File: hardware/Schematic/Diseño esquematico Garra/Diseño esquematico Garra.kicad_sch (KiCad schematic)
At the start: 14 parts, among them U2 ESP32-WROOM-32

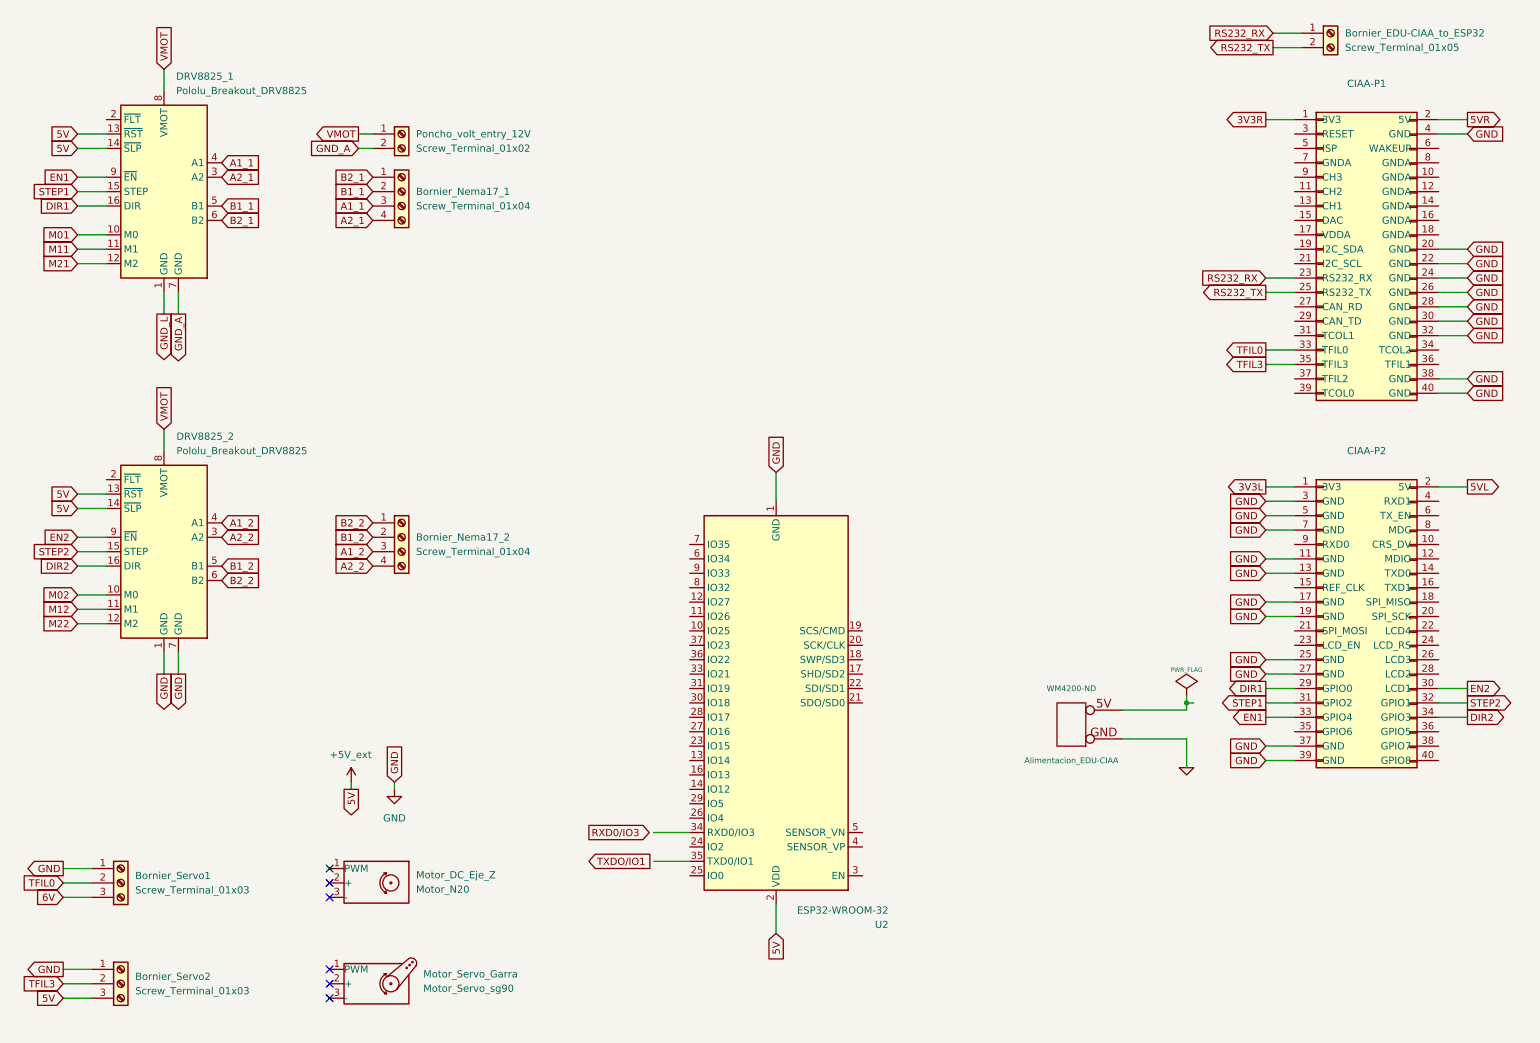
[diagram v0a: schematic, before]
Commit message: Schematics updated - pins, PowerSupply
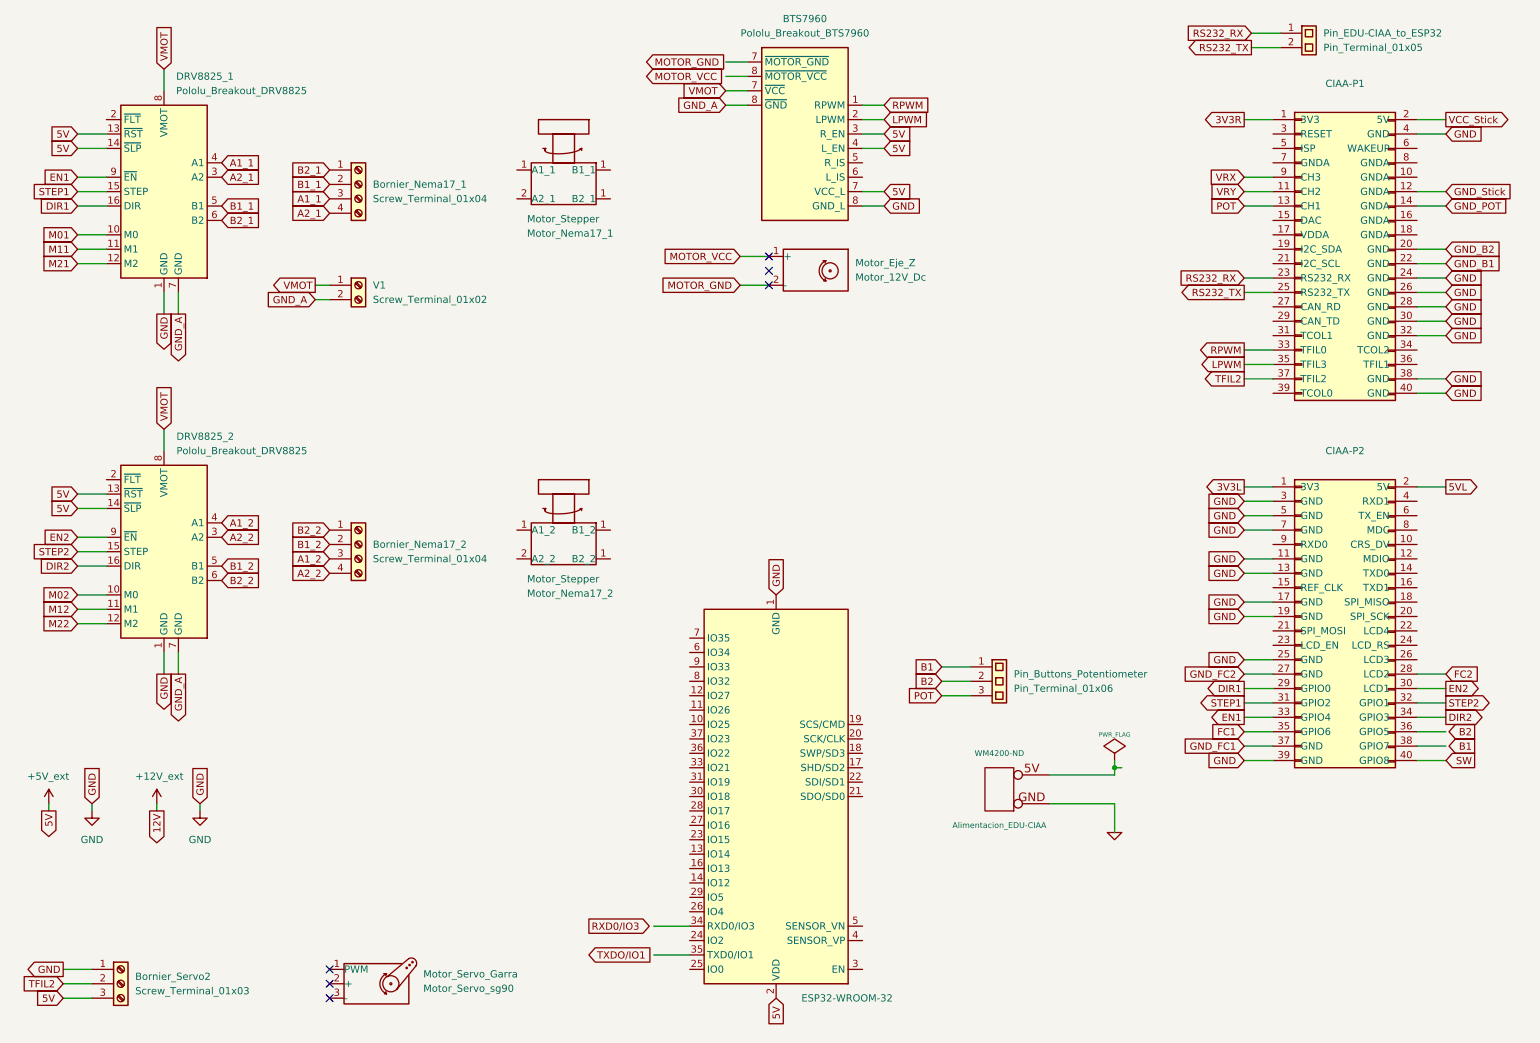
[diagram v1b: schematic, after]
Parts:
- removed Bornier_Servo1: Screw_Terminal_01x03, ProyectoTdL:TerminalBlock_bornier-3_P5.08mm, symbol Connector:Screw_Terminal_01x03
- added BTS7960: Pololu_Breakout_BTS7960, Module:Pololu_Breakout-16_15.2x20.3mm, symbol Driver_Motor:Pololu_Breakout_DRV8825
- added Motor_Stepper: Motor_Nema17_2, symbol Motor:Motor_Servo
- added Motor_Stepper: Motor_Nema17_1, symbol Motor:Motor_Servo
- added Pin_Buttons_Potentiometer: Pin_Terminal_01x06, ProyectoTdL:TerminalBlock_bornier-3_P5.08mm, symbol Connector:Screw_Terminal_01x03
- Motor_Eje_Z: renamed from Motor_DC_Eje_Z; value Motor_N20 -> Motor_12V_Dc
- Pin_EDU-CIAA_to_ESP32: renamed from Bornier_EDU-CIAA_to_ESP32; value Screw_Terminal_01x05 -> Pin_Terminal_01x05
- renumbered Poncho_volt_entry_12V to V1
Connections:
- net GND_L is gone; now on net GND: DRV8825_1.1 (GND)
- net +5V_ext: now also BTS7960.3 (R_EN), BTS7960.4 (L_EN), BTS7960.7 (VCC_L)
- net GND: now also BTS7960.8 (GND_L); no longer CIAA-P1.20 (GND), CIAA-P1.22 (GND), CIAA-P2.27 (GND), CIAA-P2.37 (GND), DRV8825_2.7 (GND)
- net GND_A: now also DRV8825_2.7 (GND), BTS7960.8 (GND_L)
- net VMOT: now also BTS7960.7 (VCC_L)
- net VRY: now reaches CIAA-P1.11 (CH2)
- net GND_Stick: now reaches CIAA-P1.12 (GNDA)
- net POT: now reaches CIAA-P1.13 (CH1)
- net POT: now also Pin_Buttons_Potentiometer.3 (Pin_3)
- net GND_POT: now reaches CIAA-P1.14 (GNDA)
- net TFIL2: now reaches CIAA-P1.37 (TFIL2)
- net TFIL2: now also Bornier_Servo2.2 (Pin_2)
- net VRX: now reaches CIAA-P1.9 (CH3)
- net MOTOR_VCC: now reaches Motor_Eje_Z.1 (+)
- net MOTOR_GND: now reaches Motor_Eje_Z.2 (-)
- net FC2: now reaches CIAA-P2.28 (LCD2)
- net FC1: now reaches CIAA-P2.35 (GPIO6)
- net 5VR renamed VCC_Stick
- net TFIL0 renamed RPWM
- net RPWM: now also BTS7960.1 (RPWM)
- net TFIL3 renamed LPWM
- net LPWM: now also BTS7960.2 (LPWM); no longer Bornier_Servo2.2 (Pin_2)
- new net B1: Pin_Buttons_Potentiometer.1 (Pin_1)
- new net B2: Pin_Buttons_Potentiometer.2 (Pin_2)
- new net GND_B1: CIAA-P1.22 (GND)
- new net GND_B2: CIAA-P1.20 (GND)
- new net GND_FC1: CIAA-P2.37 (GND)
- new net GND_FC2: CIAA-P2.27 (GND)
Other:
- moved on the sheet: Alimentacion_EDU-CIAA, Bornier_Nema17_1, Bornier_Nema17_2, CIAA-P1, CIAA-P2, V1

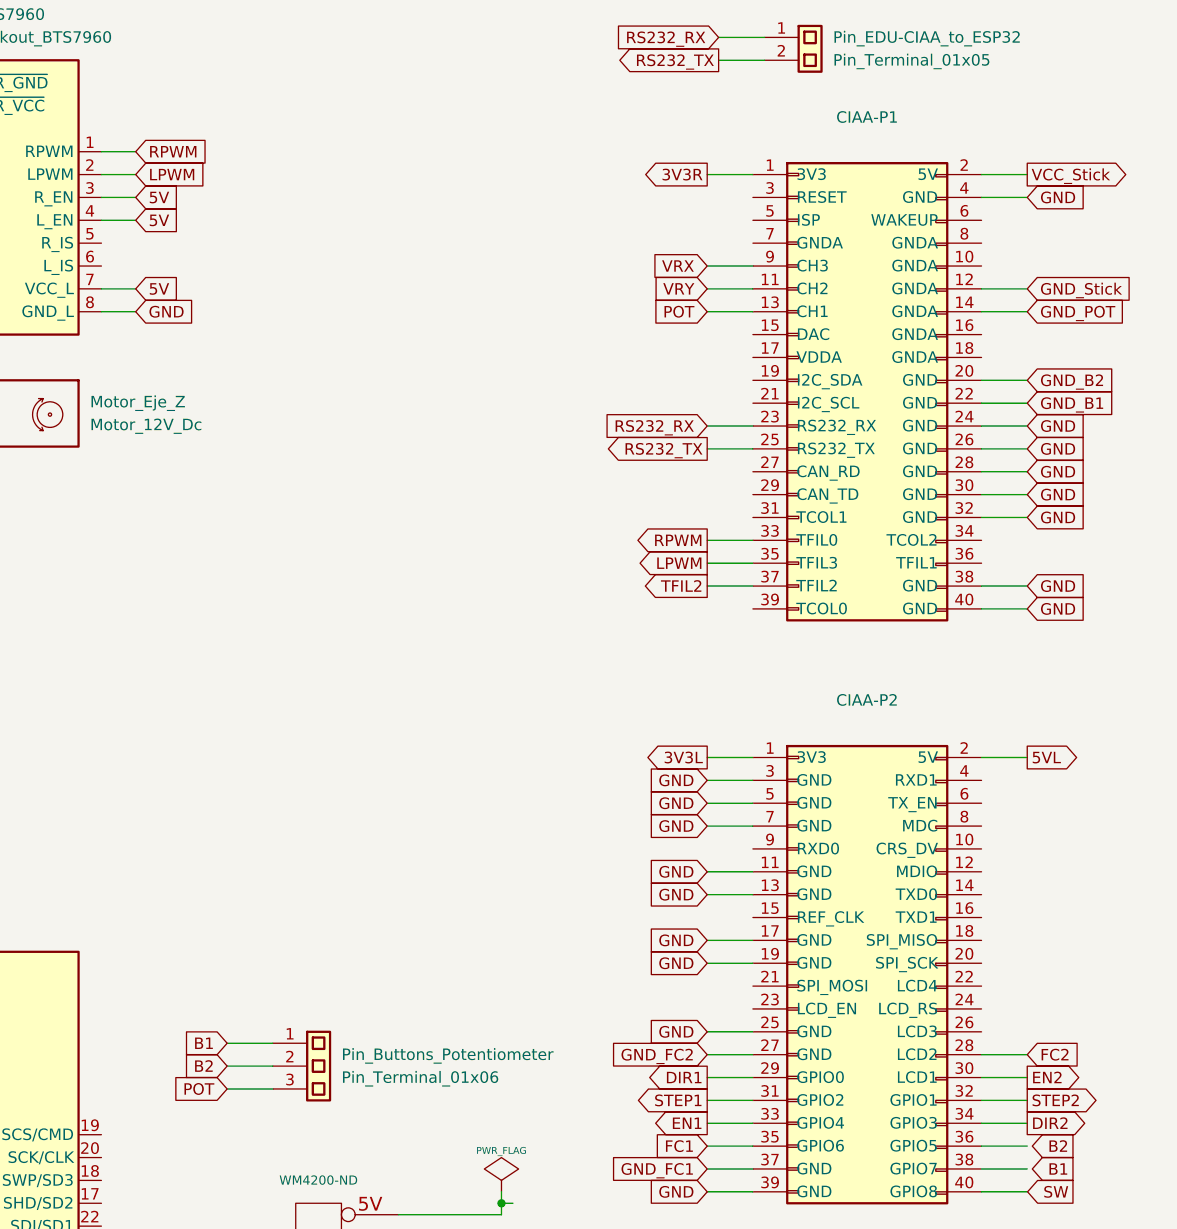
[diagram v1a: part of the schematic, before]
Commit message: Schematics updated - borniers,pins
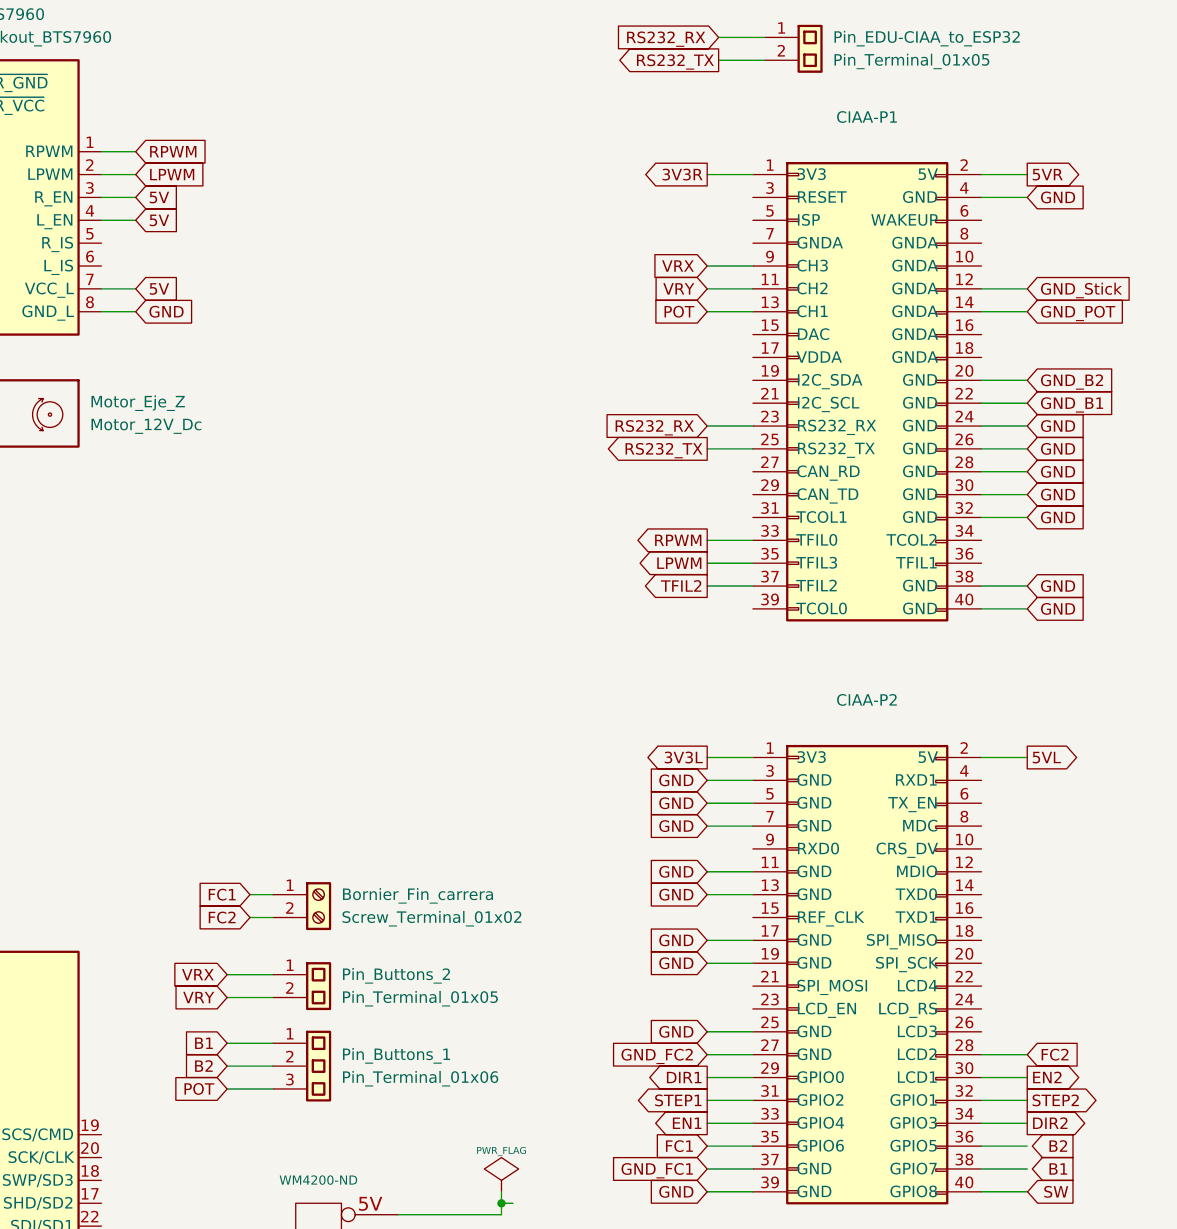
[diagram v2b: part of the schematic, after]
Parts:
- added Bornier_Fin_carrera: Screw_Terminal_01x02, ProyectoTdL:TerminalBlock_bornier-2_P5.08mm, symbol Connector:Screw_Terminal_01x02
- added Pin_Buttons_2: Pin_Terminal_01x05, ProyectoTdL:TerminalBlock_bornier-2_P5.08mm, symbol Connector:Screw_Terminal_01x02
- renumbered Pin_Buttons_Potentiometer to Pin_Buttons_1
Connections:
- net FC1: now also Bornier_Fin_carrera.1 (Pin_1)
- net FC2: now also Bornier_Fin_carrera.2 (Pin_2)
- net VRX: now also Pin_Buttons_2.1 (Pin_1)
- net VRY: now also Pin_Buttons_2.2 (Pin_2)
- net VCC_Stick renamed 5VR
